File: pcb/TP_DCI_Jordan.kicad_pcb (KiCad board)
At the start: 2 copper layers, 52 x 30 mm, 19 parts, among them J1 MICRO, J2 Display, SW1 SW_DIP_x03, U1 PCF8574

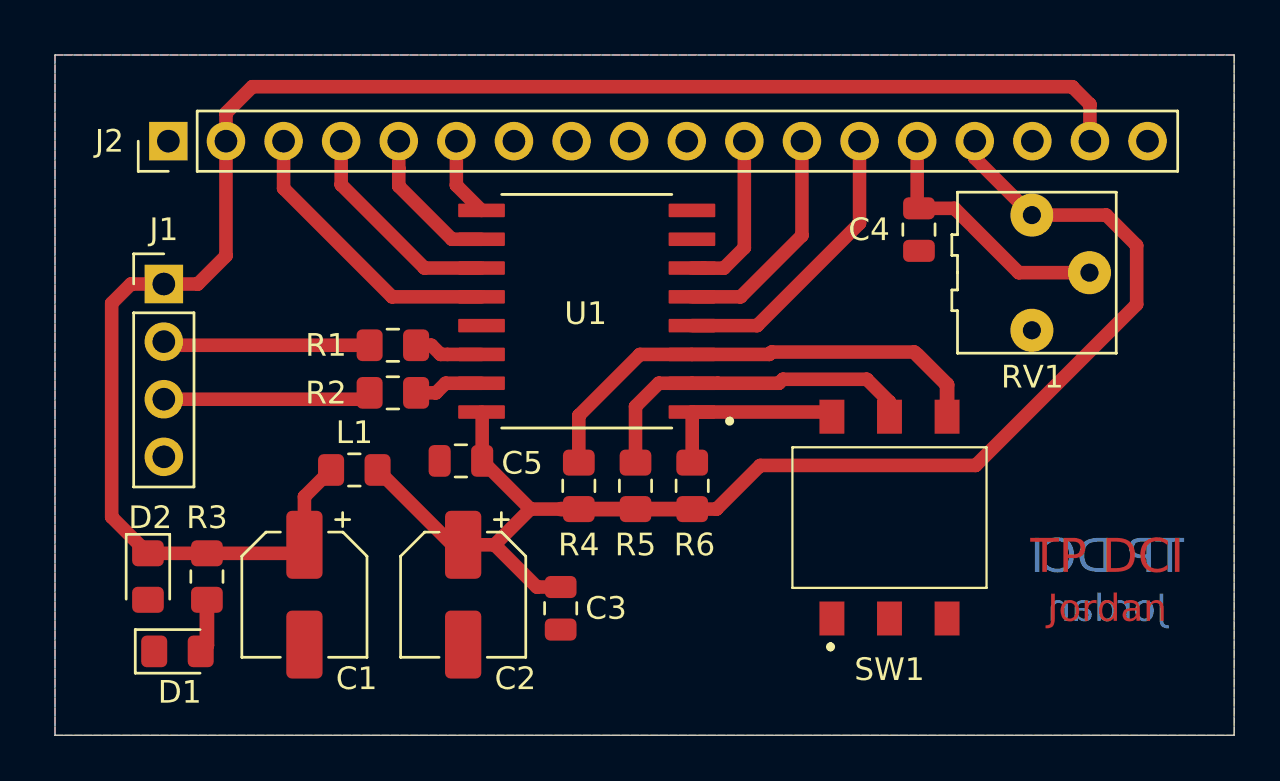
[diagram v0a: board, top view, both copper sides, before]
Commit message: minimización tamaño PCB
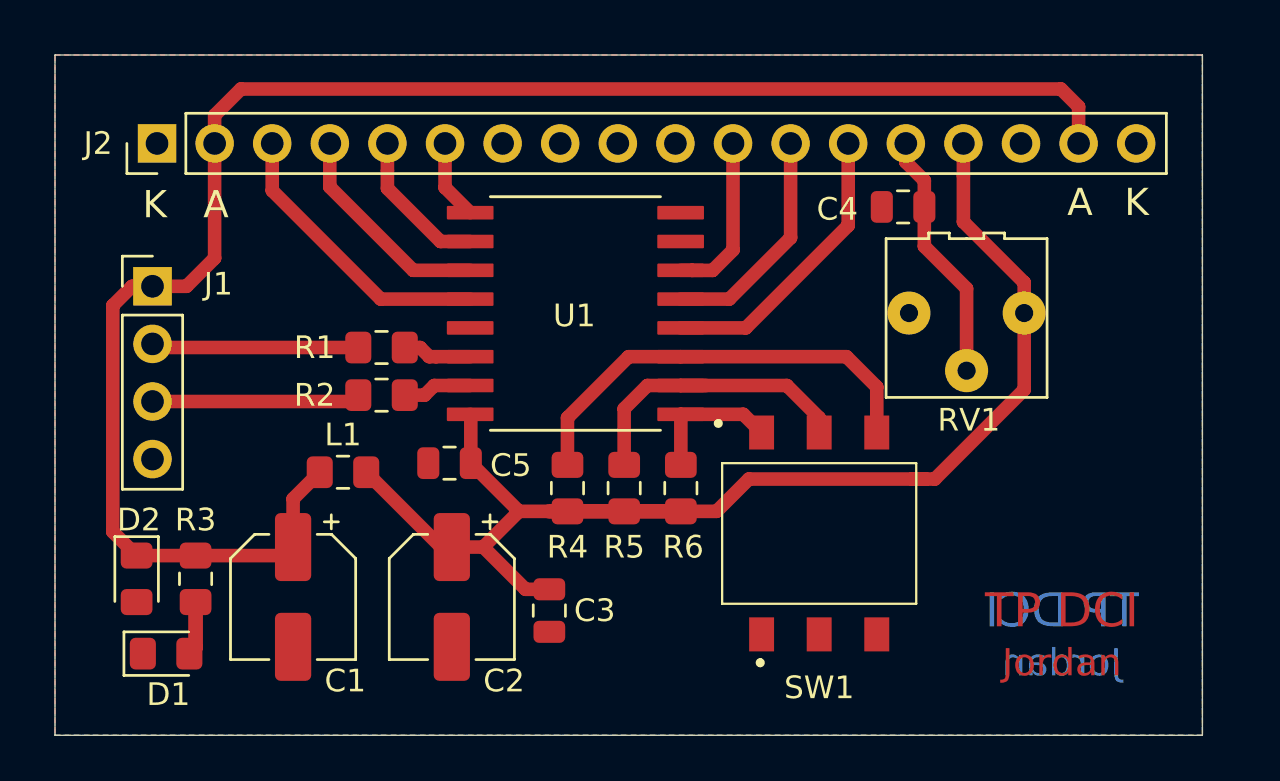
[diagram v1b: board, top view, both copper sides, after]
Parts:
- moved RV1 3.69 mm to (121.6, 122.0), turned to 0 degrees
- moved SW1 3.18 mm to (115.1, 131.5)
- moved C4 1.22 mm to (118.8, 117.1), turned to 180 degrees
- moved C1 0.51 mm to (91.9, 134.3)
- moved C2 0.51 mm to (98.9, 134.3)
- moved D1 0.51 mm to (86.3, 136.8)
- moved L1 0.51 mm to (94.1, 128.8)
- moved R2 0.51 mm to (95.8, 125.4)
- moved C3 0.51 mm to (103.2, 134.9)
- moved C5 0.51 mm to (98.8, 128.4)
- moved D2 0.51 mm to (85.0, 133.5)
- moved J1 0.51 mm to (85.7, 120.6)
- moved J2 0.51 mm to (85.9, 114.3)
- moved R1 0.51 mm to (95.8, 123.3)
- moved R3 0.51 mm to (87.6, 133.5)
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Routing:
- net VDD: track 61.0 -> 55.5 mm
- net Net-(R4-Pad1): track 23.4 -> 19.4 mm
- net Net-(R6-Pad1): track 8.50 -> 6.15 mm
- net Net-(R5-Pad1): track 15.4 -> 13.9 mm
- net /Vin: track 75.4 -> 74.6 mm
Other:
- board size 52 x 30 mm -> 50.6 x 30 mm
- board text added: "A"
- board text added: "K"

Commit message: medición longitudes de PCB
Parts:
- moved C1 0.89 mm to (91.1, 133.9)
- moved C2 0.89 mm to (98.1, 133.9)
- moved J2 0.89 mm to (85.1, 113.9)
- moved C3 0.89 mm to (102.4, 134.5)
- moved C5 0.89 mm to (98.0, 128.0)
- moved D1 0.89 mm to (85.5, 136.4)
- moved D2 0.89 mm to (84.2, 133.1)
- moved L1 0.89 mm to (93.3, 128.4)
- moved R2 0.89 mm to (95.0, 125.0)
- moved R3 0.89 mm to (86.8, 133.1)
- moved R4 0.89 mm to (103.2, 129.1)
- moved R5 0.89 mm to (105.7, 129.1)
- moved R6 0.89 mm to (108.2, 129.1)
- moved RV1 0.89 mm to (120.8, 121.6)
- moved SW1 0.89 mm to (114.3, 131.1)
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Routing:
- net Net-(R4-Pad1): track 19.4 -> 18.7 mm
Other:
- board size 50.6 x 30 mm -> 50 x 30 mm

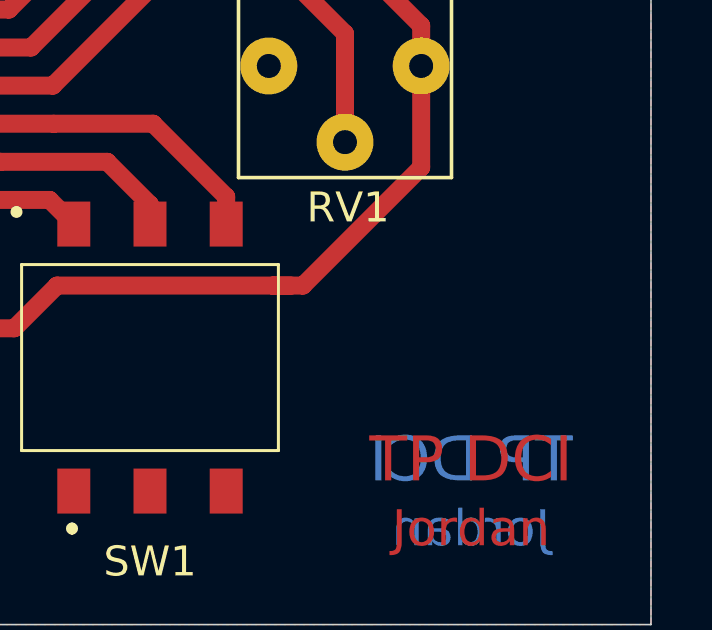
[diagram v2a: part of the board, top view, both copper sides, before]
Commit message: configuración de vías
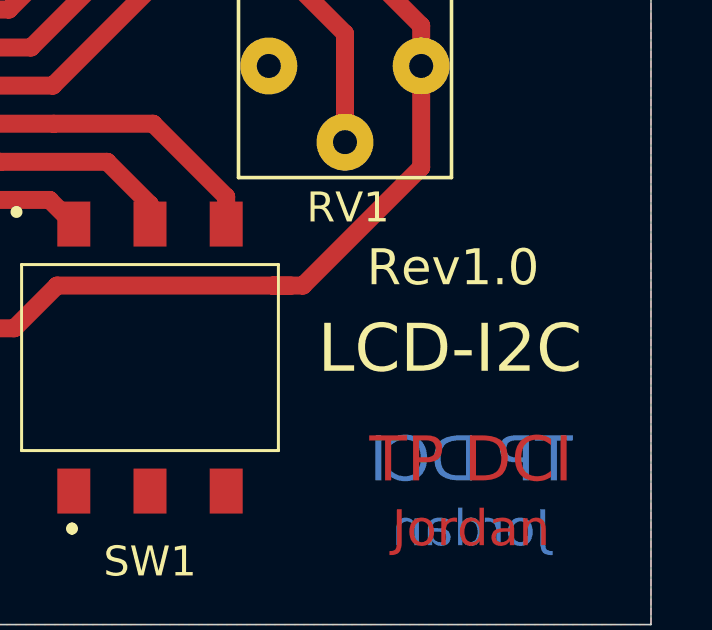
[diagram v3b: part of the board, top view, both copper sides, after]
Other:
- net class Default: via_dia 0.8 -> 1.5; via_drill 0.4 -> 0.7
- board text added: "LCD-I2C"
- board text added: "Rev1.0"
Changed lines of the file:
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@@
   (general
     (thickness 1.6)
-    (drawings 18)
+    (drawings 20)
     (tracks 106)
     (zones 0)
@@
     (zone_45_only no)
     (trace_min 0.6)
-    (via_size 0.8)
-    (via_drill 0.4)
+    (via_size 1.5)
+    (via_drill 0.7)
     (via_min_size 0.4)
     (via_min_drill 0.3)
@@
     (clearance 0.6)
     (trace_width 0.6)
-    (via_dia 0.8)
-    (via_drill 0.4)
+    (via_dia 1.5)
+    (via_drill 0.7)
     (uvia_dia 0.3)
     (uvia_drill 0.1)
@@
     )
   )
+  (gr_text Rev1.0 (at 124.4 128.1) (layer F.SilkS)
+    (effects (font (size 1.2 1.2) (thickness 0.2)))
+  )
+  (gr_text LCD-I2C (at 124.3 130.8) (layer F.SilkS)
+    (effects (font (size 1.6 1.6) (thickness 0.3)))
+  )
   (gr_line (start 82 111) (end 130 111) (layer Margin) (width 0.15))
